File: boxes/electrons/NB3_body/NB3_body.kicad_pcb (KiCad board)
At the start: 2 copper layers, 200 x 199.5 mm, 36 parts, among them J1 Conn_02x05_Counter_Clockwise, J10 Conn_02x03_Top_Bottom, J11 Conn_02x03_Top_Bottom, J12 Conn_02x03_Top_Bottom, J13 JST ZH 6-way Socket, J14 JST ZH 6-way Socket, J2 Conn_02x05_Counter_Clockwise, J3 Conn_02x05_Counter_Clockwise, J4 Conn_02x05_Counter_Clockwise, J5 Conn_02x05_Counter_Clockwise, J6 Conn_02x05_Counter_Clockwise, J7 Conn_02x05_Counter_Clockwise, J8 Conn_02x05_Counter_Clockwise, J9 JST SH 4-way Socket

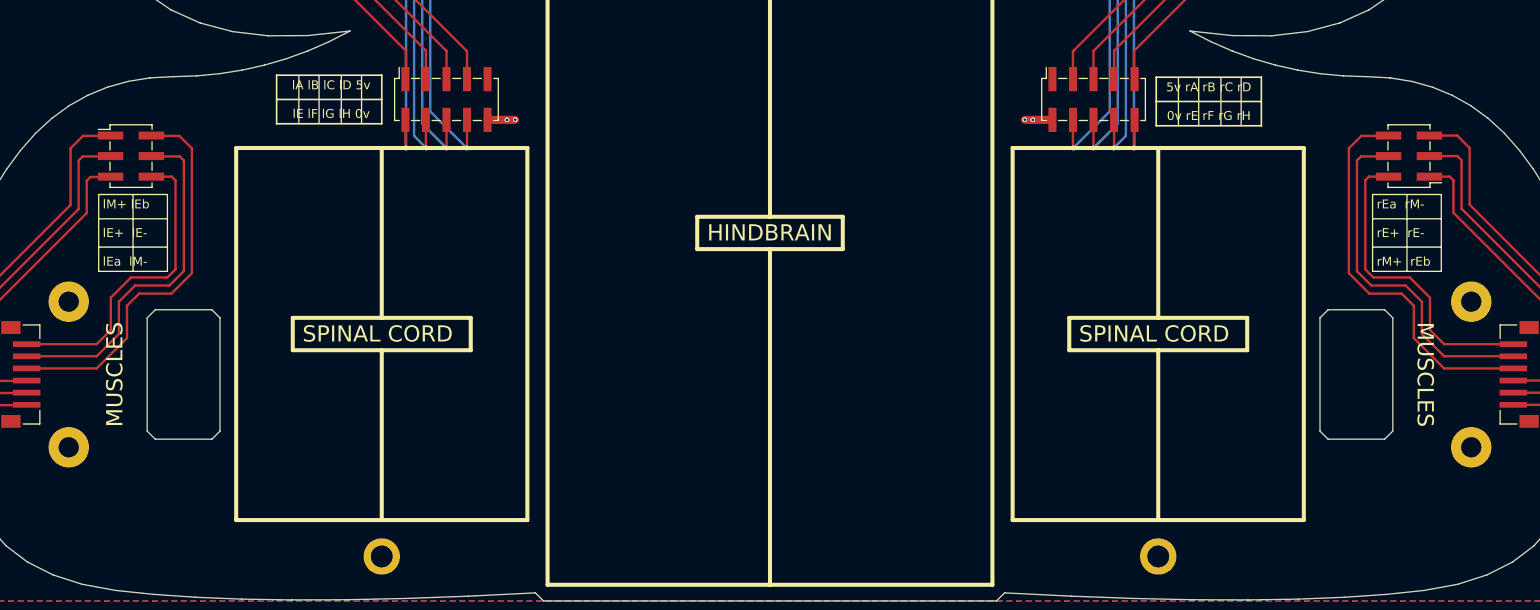
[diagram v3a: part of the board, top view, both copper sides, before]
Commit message: Update NB3 Body (for servo drive)
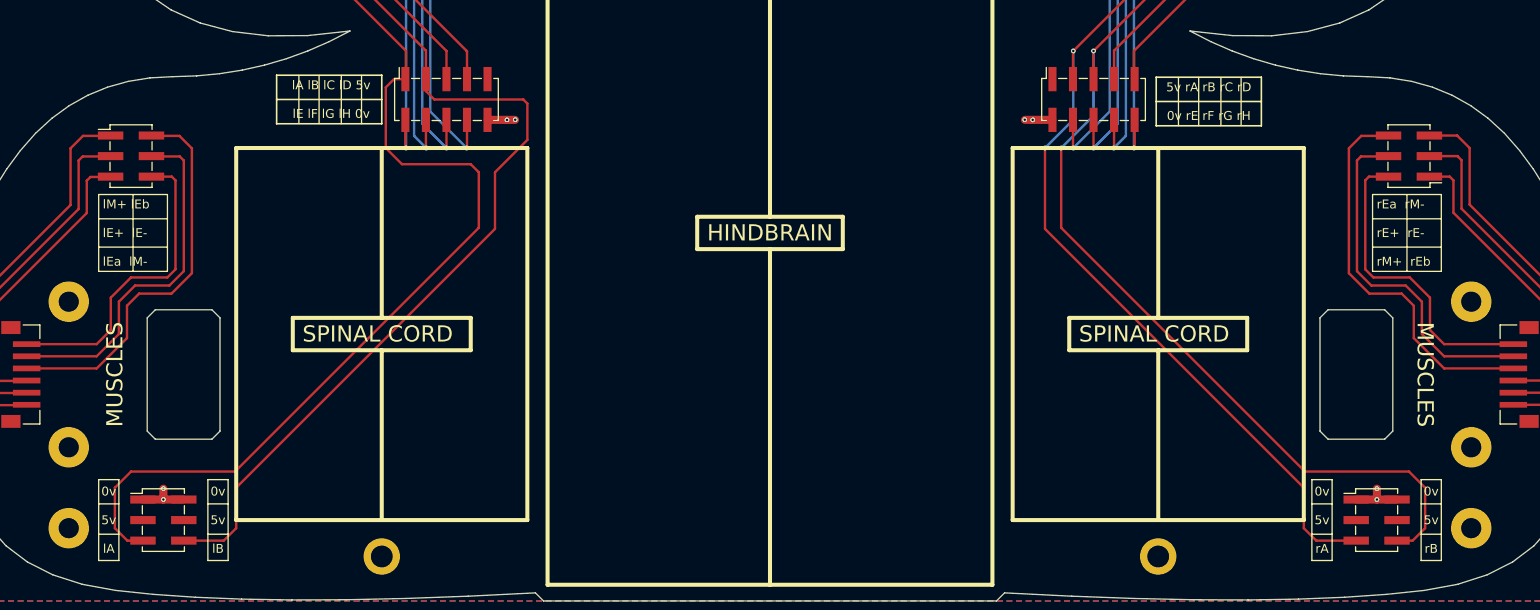
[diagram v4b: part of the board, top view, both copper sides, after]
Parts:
- removed the G*** at (124.5, 123.0)
- added H21: MountingHole, MountingHole:MountingHole_2.5mm_Pad, F.Cu at (37.8, 214.0)
- added H22: MountingHole, MountingHole:MountingHole_2.5mm_Pad, F.Cu at (211.2, 214.0)
- added J15: Conn_02x03_Top_Bottom, Connector_PinHeader_2.54mm:PinHeader_2x03_P2.54mm_Vertical_SMD, F.Cu at (49.5, 213.0)
- added J16: Conn_02x03_Top_Bottom, Connector_PinHeader_2.54mm:PinHeader_2x03_P2.54mm_Vertical_SMD, F.Cu at (199.5, 213.0)
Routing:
- net /LA: track 231.2 -> 328.5 mm
- net /RB: track 158.1 -> 249.0 mm, vias 4 -> 6
- net /LB: track 228.9 -> 318.1 mm
- net /RA: track 156.5 -> 237.3 mm, vias 4 -> 6
- net GND: track 57.1 -> 69.9 mm, vias 27 -> 31
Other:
- board text added: "0v 5v lA"
- board text added: "0v 5v lB"
- board text added: "0v 5v rA"
- board text added: "0v 5v rB"
- board text added: "NB3_body Rev 0.0.3"
- board text removed: "NB3_body Rev 0.0.2"

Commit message: Update NB3 PCBs and parts
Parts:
- removed the G*** at (124.5, 116.0)
- added G***: LOGO, NB3_body:Logo_NBB_30mm, F.Cu at (124.5, 117.0)

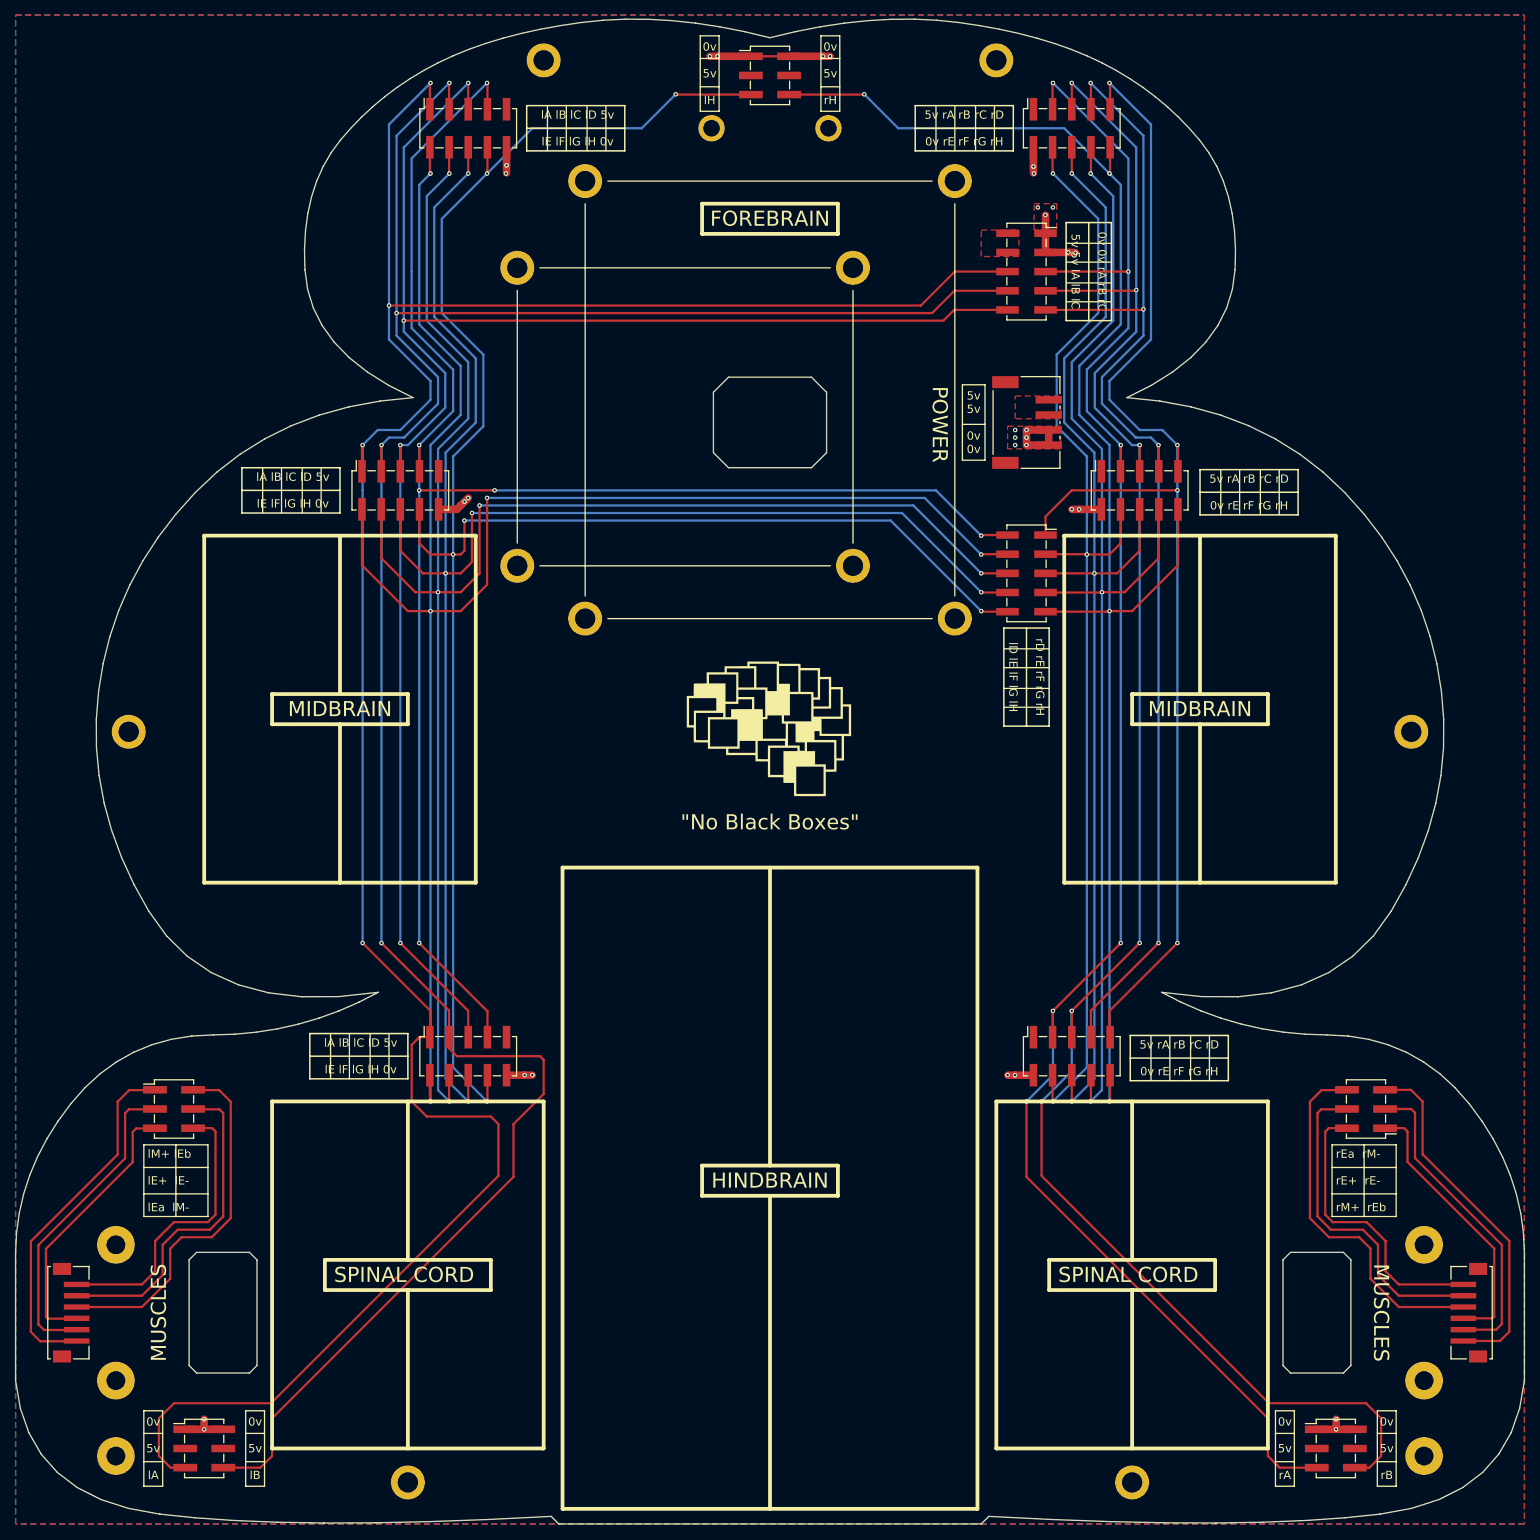
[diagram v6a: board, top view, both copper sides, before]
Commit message: Work on NB3_bidy (v4) - TT DC motors
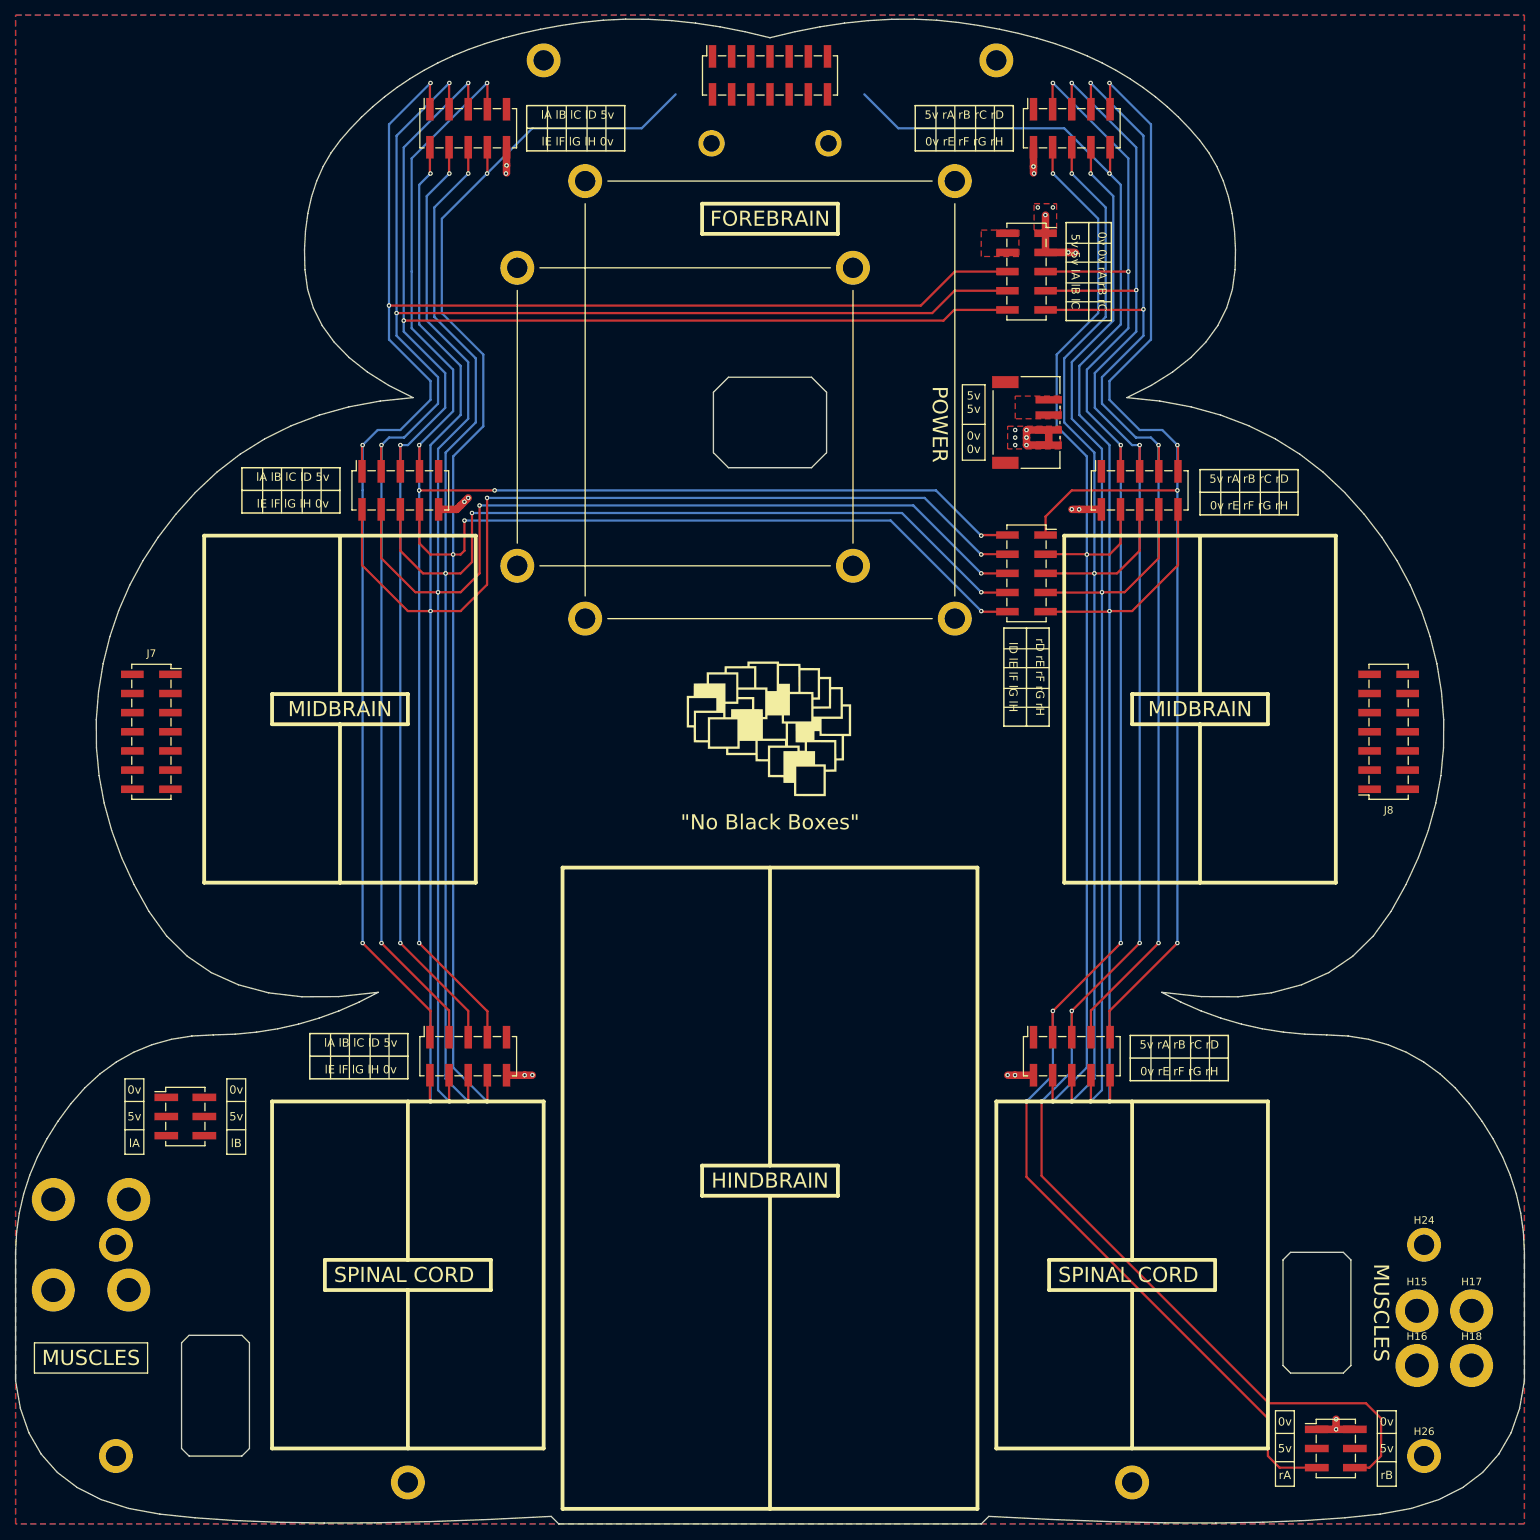
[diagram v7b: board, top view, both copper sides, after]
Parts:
- removed the H19 at (39.5, 118.0)
- removed the H20 at (209.5, 118.0)
- removed the J10 at (124.5, 31.0)
- removed J11: Conn_02x03_Top_Bottom, Connector_PinHeader_2.54mm:PinHeader_2x03_P2.54mm_Vertical_SMD
- removed the J12 at (203.5, 168.0)
- removed the J13 at (31.5, 195.0)
- removed the J14 at (217.5, 195.0)
- added H13: MountingHole, MountingHole:MountingHole_3.2mm_M3_ISO7380_Pad, F.Cu at (39.5, 180.0)
- added H14: MountingHole, MountingHole:MountingHole_3.2mm_M3_ISO7380_Pad, F.Cu at (39.5, 192.0)
- added H15: MountingHole, MountingHole:MountingHole_3.2mm_M3_ISO7380_Pad, F.Cu at (210.2, 194.8)
- added H16: MountingHole, MountingHole:MountingHole_3.2mm_M3_ISO7380_Pad, F.Cu at (210.2, 202.0)
- added H17: MountingHole, MountingHole:MountingHole_3.2mm_M3_ISO7380_Pad, F.Cu at (217.5, 194.8)
- added H18: MountingHole, MountingHole:MountingHole_3.2mm_M3_ISO7380_Pad, F.Cu at (217.5, 202.0)
- added J7: Conn_02x07_Odd_Even, Connector_PinSocket_2.54mm:PinSocket_2x07_P2.54mm_Vertical_SMD, F.Cu at (42.5, 118.0)
- added J8: Conn_02x07_Odd_Even, Connector_PinSocket_2.54mm:PinSocket_2x07_P2.54mm_Vertical_SMD, F.Cu at (206.5, 118.0)
- added J9: Conn_02x07_Odd_Even, Connector_PinSocket_2.54mm:PinSocket_2x07_P2.54mm_Vertical_SMD, F.Cu at (124.5, 31.0)
- H11, H12: footprint MountingHole:MountingHole_2.5mm_Pad -> MountingHole:MountingHole_3.2mm_M3_ISO7380_Pad
- H23: renamed from H9; footprint MountingHole:MountingHole_2.5mm_Pad -> MountingHole:MountingHole_2.7mm_M2.5_ISO7380_Pad
- H24: renamed from H10; footprint MountingHole:MountingHole_2.5mm_Pad -> MountingHole:MountingHole_2.7mm_M2.5_ISO7380_Pad
- H25: renamed from H21; footprint MountingHole:MountingHole_2.5mm_Pad -> MountingHole:MountingHole_2.7mm_M2.5_ISO7380_Pad
- H26: renamed from H22; footprint MountingHole:MountingHole_2.5mm_Pad -> MountingHole:MountingHole_2.7mm_M2.5_ISO7380_Pad
- moved H12 182.1 mm to (29.5, 192.0)
- moved J12 44.1 mm to (47.0, 169.0)
- moved H11 25.4 mm to (29.5, 180.0)
- moved H10 2.00 mm to (132.2, 40.0)
- moved H9 2.00 mm to (116.8, 40.0)
- renumbered H5 to H1, H18 to H10, H1 to H19, H6 to H2, H2 to H20, H3 to H21, H4 to H22, H7 to H3, H8 to H4, H15 to H5, H16 to H6, H13 to H7, H14 to H8, H17 to H9, J9 to J10, J15 to J12, J16 to J13, J7 to J14, J8 to J15
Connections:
- J14 pad 10: /LC -> /SDI
- J14 pad 5: /RA -> /WS
- J14 pad 6: /LA -> /SCK
- J14 pad 7: /RB -> /GAIN
- J14 pad 8: /LB -> +3V3
- J14 pad 9: /RC -> /SDO
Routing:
- net /LA: track 328.5 -> 231.2 mm
- net /LB: track 318.1 -> 228.9 mm
- net /RE A: track 48.7 -> 0.00 mm
- net /LE B: track 48.7 -> 0.00 mm
- net /LM+: track 47.5 -> 0.00 mm
- net /RM-: track 47.5 -> 0.00 mm
- net /RE+: track 44.0 -> 0.00 mm
- net /LE-: track 44.0 -> 0.00 mm
- net /LE+: track 42.4 -> 0.00 mm
- net /RE-: track 42.4 -> 0.00 mm
- net /RM+: track 38.7 -> 0.00 mm
- net /LM-: track 38.7 -> 0.00 mm
- net /RE B: track 36.6 -> 0.00 mm
- net /LE A: track 36.6 -> 0.00 mm
- net GND: track 69.9 -> 47.6 mm, vias 31 -> 25
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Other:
- outline, holes or cut-outs redrawn
- board text added: "NB3_body Rev 0.0.4 For Research and Education ONLY"
- board text removed: "0v 5v lH"
- board text removed: "0v 5v rH"
- board text removed: "NB3_body Rev 0.0.3"
- board text removed: "lM+ lEb lE+ lE- lEa lM-"
- board text removed: "rEa rM- rE+ rE- rM+ rEb"
